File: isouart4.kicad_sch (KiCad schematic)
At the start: 27 parts, among them J1 USB_B, J2 Conn_01x04, J3 Conn_01x04, J4 Conn_01x04, J5 Conn_01x04, U1 LP2950CDT-3.3, U2 π122U31, U3 π122U31, U4 π122U31, U5 π122U31

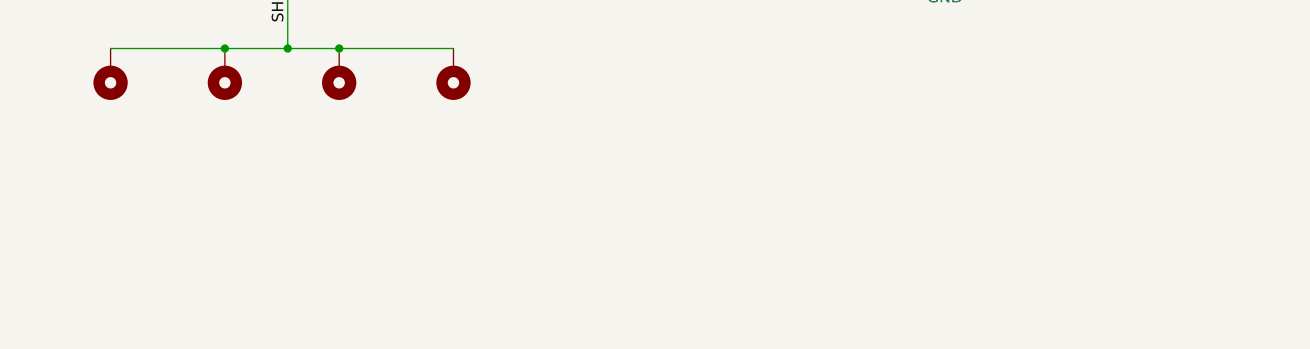
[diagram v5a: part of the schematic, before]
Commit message: Adjust OSHW logo to have footprint and use it
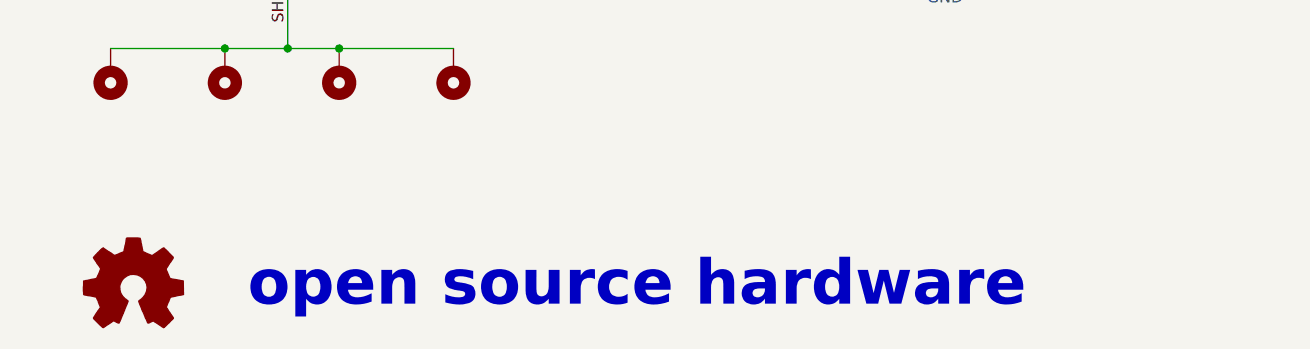
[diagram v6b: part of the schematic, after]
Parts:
- added LOGO1: OSHW, isouart4:OSHW, symbol isouart4:OSHW
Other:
- note added: "open source hardware"
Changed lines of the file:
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@@
     (stroke (width 0) (type default))
+  )
+  (text "open source hardware" (at 45.085 184.785 0)
+    (effects (font (size 5 5) (thickness 0.6) bold) (justify left bottom))
   )
   (text "Connectors, 3.3V regulator and isolators" (at 182.245 175.895 0)
@@
         )
       )
+    )
+  )
+  (symbol (lib_id "isouart4:OSHW") (at 32.385 182.245 0) (unit 1)
+    (in_bom no) (on_board yes) (dnp no) (fields_autoplaced)
+    (property "Reference" "LOGO1" (at 32.385 175.26 0)
+      (effects (font (size 1.27 1.27)) hide)
+    )
+    (property "Value" "OSHW" (at 32.385 187.96 0)
+      (effects (font (size 1.27 1.27)) hide)
+    )
+    (property "Footprint" "isouart4:OSHW" (at 32.385 182.245 0)
+      (effects (font (size 1.27 1.27)) hide)
+    )
+    (property "Datasheet" "~" (at 32.385 182.245 0)
+      (effects (font (size 1.27 1.27)) hide)
+    )
+    (property "Sim.Enable" "0" (at 32.385 182.245 0)
+      (effects (font (size 1.27 1.27)) hide)
+    )
+    (instances
+      (project "isouart4"
+        (path "/7c54d849-3d49-4f8e-b560-9dd1d738085c"
+          (reference "LOGO1") (unit 1)
+        )
+      )

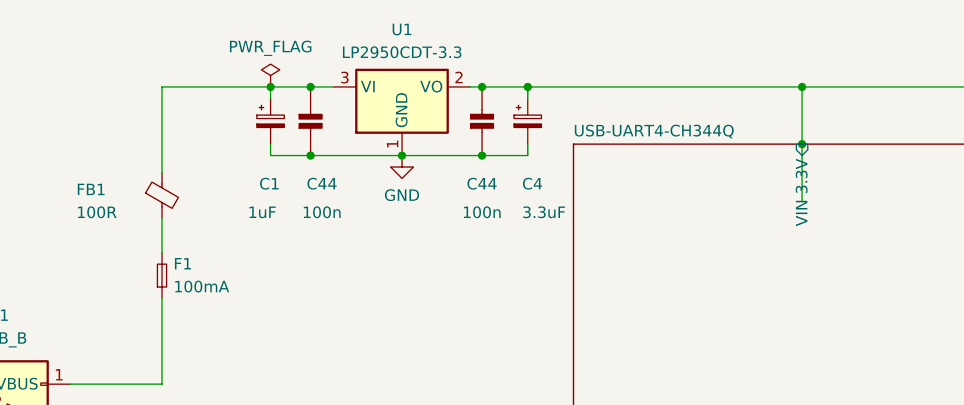
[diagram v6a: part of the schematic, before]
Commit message: adjust regulator tantalum capacitors (1+3.3uF -> 3x2.2uF)
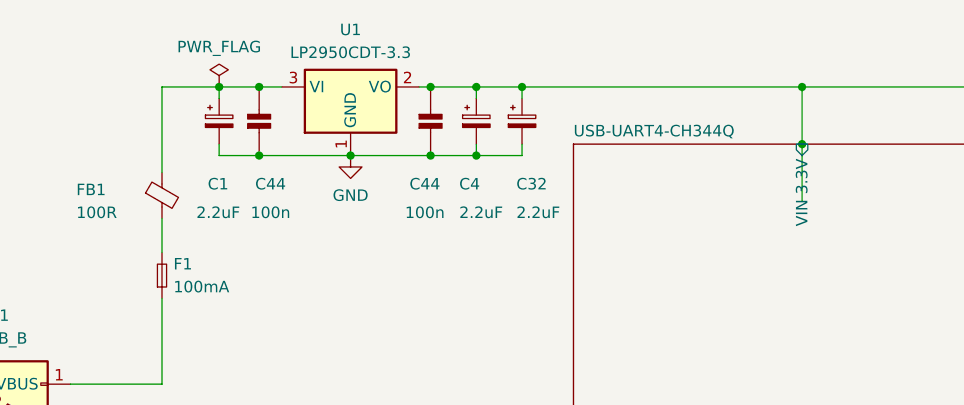
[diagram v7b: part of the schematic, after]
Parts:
- added C32: 2.2uF, Capacitor_Tantalum_SMD:CP_EIA-3528-15_AVX-H_Pad1.50x2.35mm_HandSolder, symbol Device:C_Polarized_Small
- C1: value 1uF -> 2.2uF
- C4: value 3.3uF -> 2.2uF
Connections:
- net GND: now also C32.2
- net USB-UART4-CH344Q/VIN 3.3V: now also C32.1
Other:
- moved on the sheet: C1, C4, C44, U1

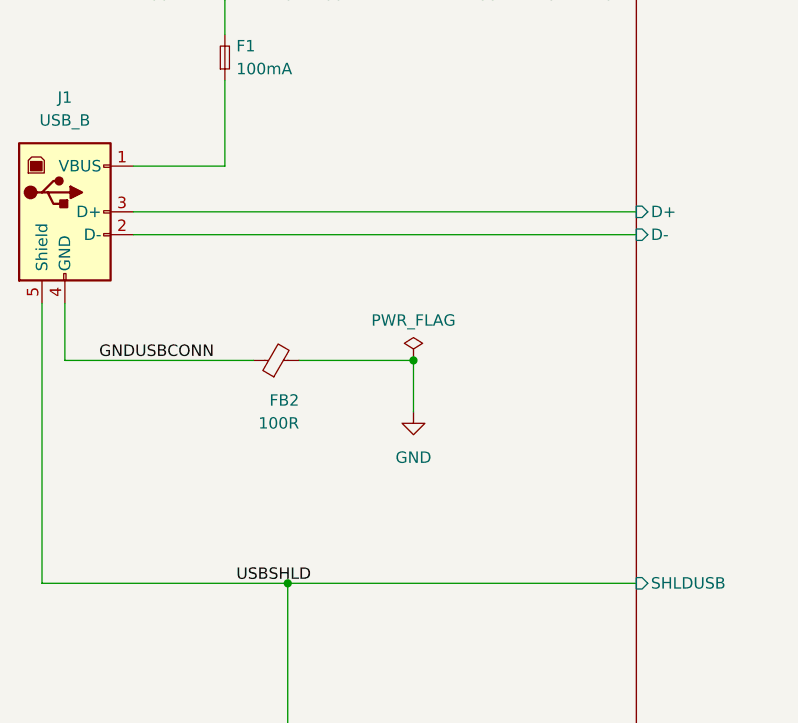
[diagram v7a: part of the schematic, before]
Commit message: rework ESD protection (handsolder sot-23 on USB connector)
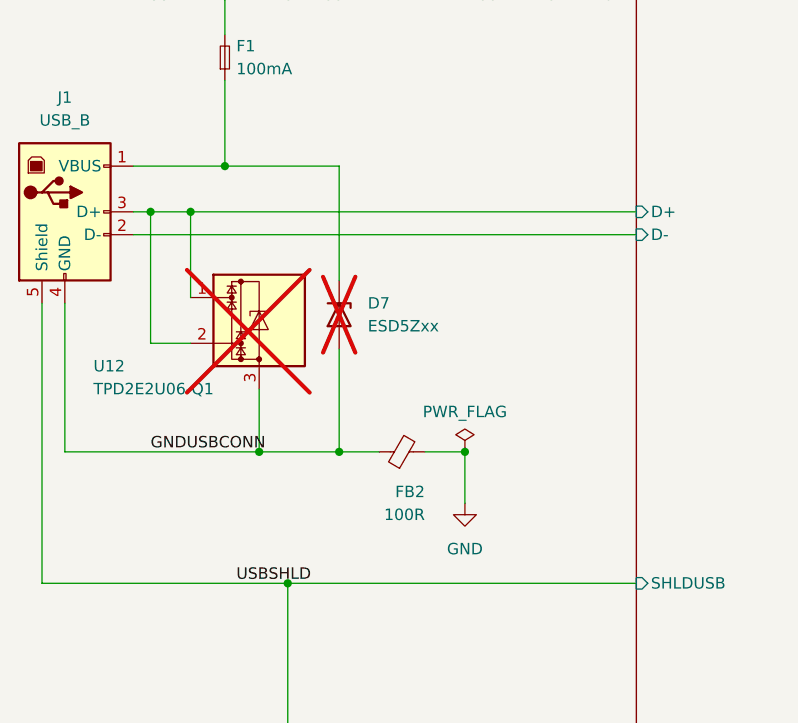
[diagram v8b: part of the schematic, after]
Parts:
- added D7: ESD5Zxx, Diode_SMD:D_SOD-523, symbol Diode:ESD5Zxx
- added U12: TPD2E2U06-Q1, Package_TO_SOT_SMD:SOT-23_Handsoldering, symbol isouart4:TPD2E2U06-Q1
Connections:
- net GNDUSBCONN: now also D7.2 (A), U12.3
- net USB-UART4-CH344Q/D+: now also U12.1, U12.2
- net at F1.1, J1.1 (VBUS): now also D7.1 (K)
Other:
- moved on the sheet: FB2
